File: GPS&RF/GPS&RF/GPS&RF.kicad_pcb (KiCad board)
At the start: 2 copper layers, 52.8 x 49.5 mm, 13 parts, among them IC1 FGPMMOPA6H, J1 U.FL-R-SMT(10), J2 Conn_01x13_Male, U1 LAMBDA-9S-Global

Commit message: COMPLETED RF&GPS BOARD!
hoooorahhhh
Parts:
- C1: moved to B.Cu
- C2: moved to F.Cu
- moved U1 63.7 mm to (144.6, 133.4), turned to 90 degrees
- moved J1 53.4 mm to (131.5, 98.6), turned to 180 degrees
- moved C1 48.4 mm to (148.5, 130.8), turned to 0 degrees
- moved IC1 38.3 mm to (139.8, 113.0)
- moved J2 34.0 mm to (133.4, 103.3)
- moved R1 33.6 mm to (137.1, 98.7)
- moved C2 33.0 mm to (159.9, 106.5), turned to 0 degrees
- moved D1 32.9 mm to (135.2, 98.7), turned to 270 degrees
- moved AE1 31.2 mm to (132.7, 127.7)
- moved C3 28.4 mm to (160.0, 112.1), turned to 180 degrees
- moved FB1 26.6 mm to (160.0, 108.3), turned to 0 degrees
- moved C4 25.8 mm to (160.0, 110.2), turned to 180 degrees
- moved BT1 16.9 mm to (176.5, 115.2), turned to 270 degrees
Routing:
- net GND: track 113.2 -> 19.2 mm, vias 2 -> 9
- net +3V3: track 11.9 -> 67.6 mm, vias 1 -> 2
- net Net-(AE1-Pad1): track 44.4 -> 14.3 mm, vias 2 -> 0
- net /RX_D1: track 6.11 -> 31.0 mm, vias 0 -> 1
- net /GPSRST: track 47.3 -> 22.9 mm, vias 2 -> 1
- net /TX_D2: track 46.8 -> 26.4 mm, vias 2 -> 1
- net /1PPS: track 34.7 -> 14.6 mm, vias 2 -> 0
- net /RX_D2: track 44.8 -> 25.3 mm, vias 2 -> 1
- net /TX_D1: track 12.3 -> 28.0 mm, vias 2 -> 1
- net /CS: track 27.2 -> 12.8 mm
- net /MOSI: track 27.5 -> 16.5 mm
- net /MISO: track 27.3 -> 19.2 mm
- net Net-(BT1-Pad+1): track 32.5 -> 24.6 mm, vias 2 -> 0
- net /SCK: track 27.8 -> 21.9 mm
- net Net-(C3-Pad2): track 11.8 -> 7.21 mm
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- added copper zone on B.Cu, net GND
- added copper zone on F.Cu, net GND
- removed copper zone on F.Cu, net +3V3
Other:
- board size 52.8 x 49.5 mm -> 60.3 x 41.2 mm
- board text added: "HOLA"
- board text added: "RF & GPS"

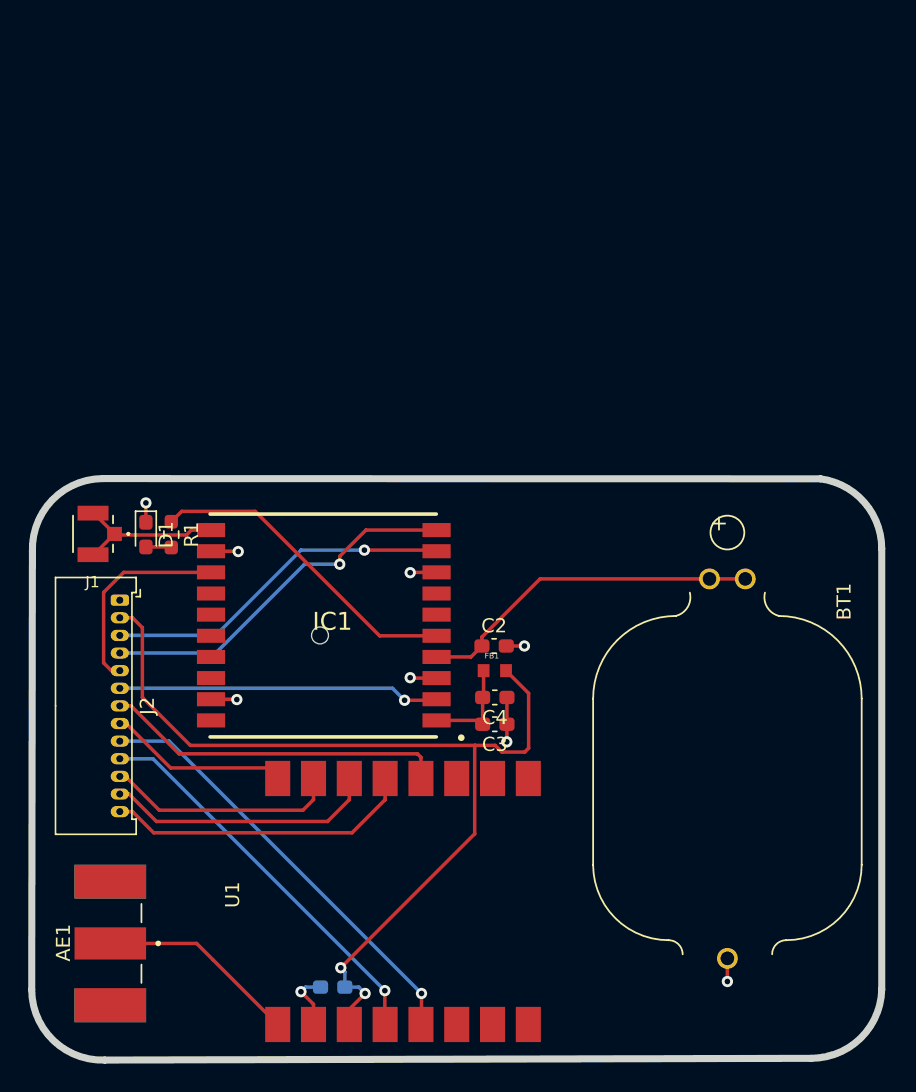
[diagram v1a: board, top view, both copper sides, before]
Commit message: Fixed up the Silkscreen layer
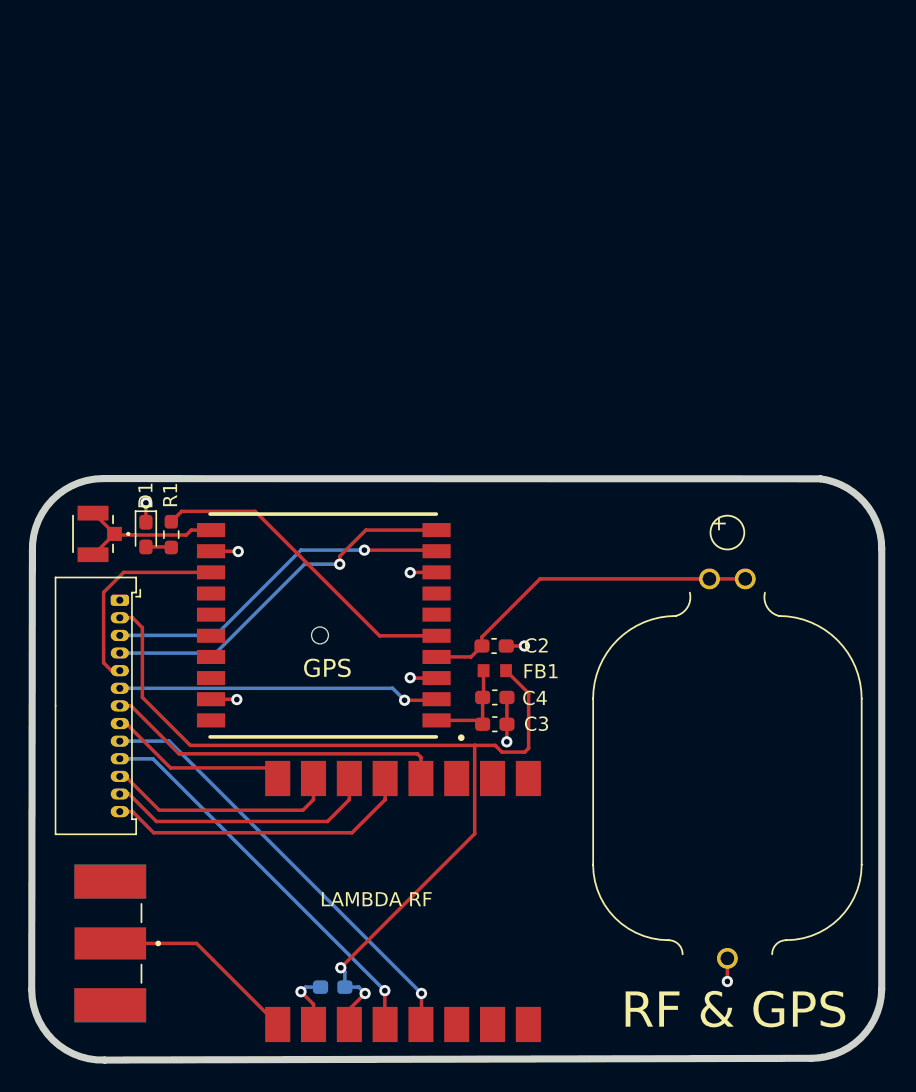
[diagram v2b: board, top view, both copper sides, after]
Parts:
-  : renamed from J2
-  : renamed from J1
-  : renamed from BT1
-  : renamed from AE1
-  LAMBDA RF: renamed from U1
- renumbered IC1 to GPS
